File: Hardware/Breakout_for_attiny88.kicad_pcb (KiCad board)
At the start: 2 copper layers, 22.9 x 46.5 mm, 14 parts, among them J1 Conn_01x08, J2 Conn_01x08, J3 Conn_01x08, J4 AVR-ISP-6, J5 Conn_01x02, J6 Conn_01x02, SW1 SW, U1 ATT88

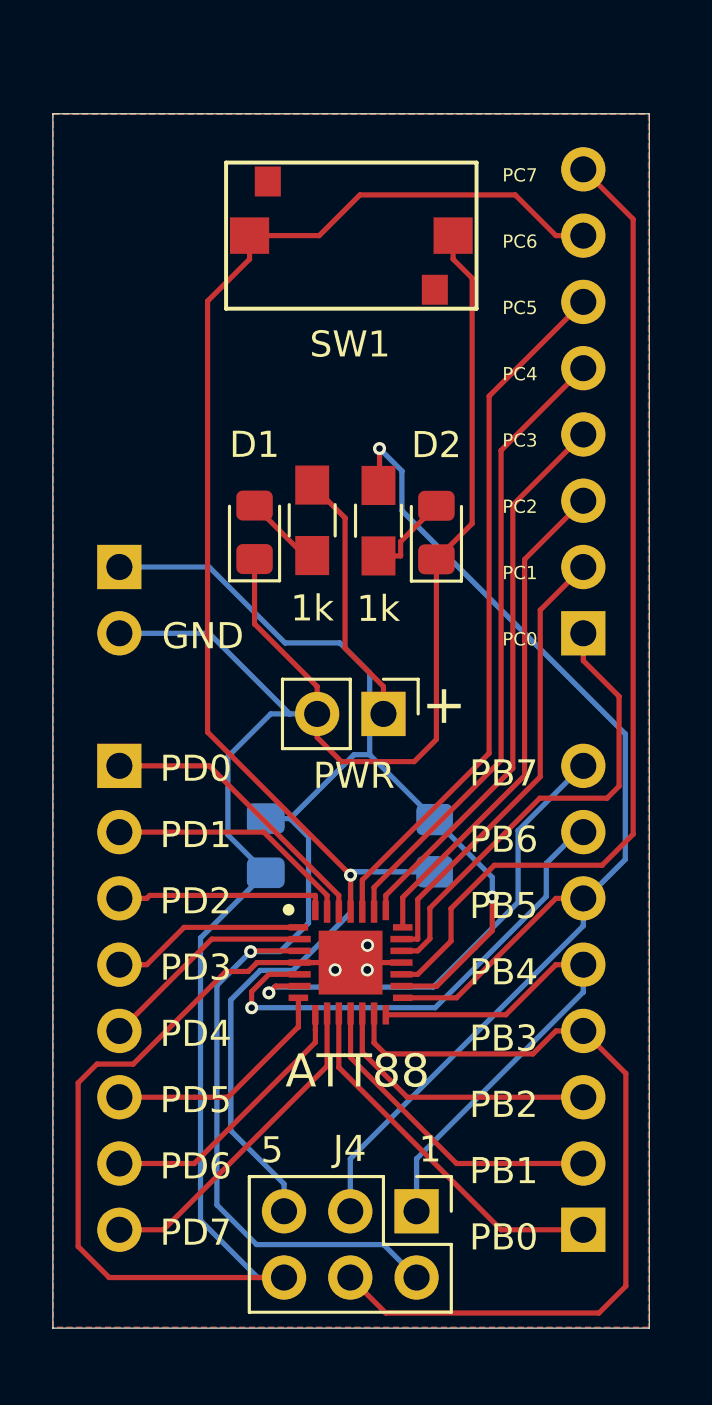
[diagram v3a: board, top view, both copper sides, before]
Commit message: pcb changed to add port pins on each header
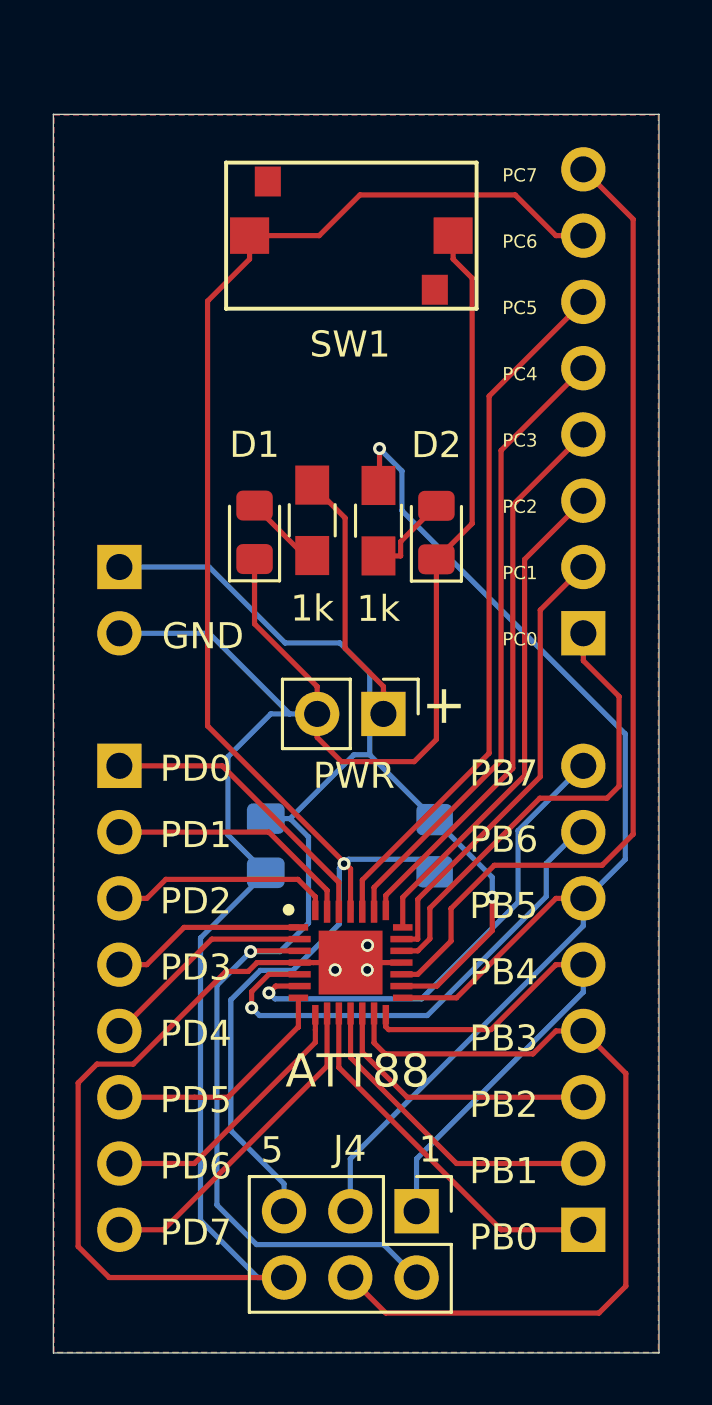
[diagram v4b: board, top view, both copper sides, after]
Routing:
- net PC6: track 62.6 -> 63.4 mm
- net MISO: track 20.5 -> 21.2 mm
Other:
- board size 22.9 x 46.5 mm -> 23.2 x 47.5 mm
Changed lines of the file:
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@@
     )
   )
-  (gr_line (start 137.06 126.55) (end 159.92 126.55) (layer "Edge.Cuts") (width 0.05))
-  (gr_line (start 159.92 80.01) (end 137.06 80.01) (layer "Edge.Cuts") (width 0.05))
-  (gr_line (start 137.06 80.01) (end 137.06 126.55) (layer "Edge.Cuts") (width 0.05))
-  (gr_line (start 159.92 80.01) (end 159.92 126.55) (layer "Edge.Cuts") (width 0.05))
+  (gr_rect (start 137.08 80.03) (end 160.29 127.5) (layer "Edge.Cuts") (width 0.0254) (fill none))
   (gr_text "PB4" (at 154.34 112.91) (layer "F.SilkS")
     (effects (font (size 1 1) (thickness 0.15)))
@@
   (segment (start 145.34 113.7) (end 145.6 113.44) (width 0.2) (layer "F.Cu") (net 9))
   (via (at 145.34 113.7) (size 0.5) (layers "F.Cu" "B.Cu") (net 9))
-  (segment (start 145.5622 113.4778) (end 145.34 113.7) (width 0.2) (layer "B.Cu") (net 9))
-  (segment (start 151.6422 113.4778) (end 145.5622 113.4778) (width 0.2) (layer "B.Cu") (net 9))
+  (segment (start 157.37 105) (end 154.89 107.48) (width 0.2) (layer "B.Cu") (net 9))
+  (segment (start 157.39 105) (end 157.37 105) (width 0.2) (layer "B.Cu") (net 9))
   (segment (start 154.89 107.48) (end 154.89 110.23) (width 0.2) (layer "B.Cu") (net 9))
-  (segment (start 157.39 105) (end 157.37 105) (width 0.2) (layer "B.Cu") (net 9))
-  (segment (start 157.37 105) (end 154.89 107.48) (width 0.2) (layer "B.Cu") (net 9))
-  (segment (start 154.89 110.23) (end 151.6422 113.4778) (width 0.2) (layer "B.Cu") (net 9))
+  (segment (start 145.57 113.93) (end 145.34 113.7) (width 0.2) (layer "B.Cu") (net 9))
+  (segment (start 151.19 113.93) (end 145.57 113.93) (width 0.2) (layer "B.Cu") (net 9))
+  (segment (start 154.89 110.23) (end 151.19 113.93) (width 0.2) (layer "B.Cu") (net 9))
   (segment (start 145.34 112.99) (end 144.68 113.65) (width 0.2) (layer "F.Cu") (net 10))
   (segment (start 144.68 113.65) (end 144.68 114.27) (width 0.2) (layer "F.Cu") (net 10))
   (segment (start 146.52 112.99) (end 145.34 112.99) (width 0.2) (layer "F.Cu") (net 10))
   (via (at 144.68 114.27) (size 0.5) (layers "F.Cu" "B.Cu") (net 10))
+  (segment (start 151.4103 114.57) (end 144.98 114.57) (width 0.2) (layer "B.Cu") (net 10))
+  (segment (start 155.97 108.74) (end 155.97 110.0103) (width 0.2) (layer "B.Cu") (net 10))
+  (segment (start 155.97 110.0103) (end 151.4103 114.57) (width 0.2) (layer "B.Cu") (net 10))
   (segment (start 157.39 107.54) (end 157.17 107.54) (width 0.2) (layer "B.Cu") (net 10))
+  (segment (start 144.98 114.57) (end 144.68 114.27) (width 0.2) (layer "B.Cu") (net 10))
   (segment (start 157.17 107.54) (end 155.97 108.74) (width 0.2) (layer "B.Cu") (net 10))
-  (segment (start 155.97 110.0103) (end 151.7103 114.27) (width 0.2) (layer "B.Cu") (net 10))
-  (segment (start 151.7103 114.27) (end 144.68 114.27) (width 0.2) (layer "B.Cu") (net 10))
-  (segment (start 155.97 108.74) (end 155.97 110.0103) (width 0.2) (layer "B.Cu") (net 10))
-  (segment (start 142.99 103.709) (end 142.99 87.1903) (width 0.2) (layer "F.Cu") (net 11))
+  (segment (start 148.47 108.95) (end 142.99 103.47) (width 0.2) (layer "F.Cu") (net 11))
+  (segment (start 144.6 85.5803) (end 144.6 84.68) (width 0.2) (layer "F.Cu") (net 11))
+  (segment (start 142.99 87.1903) (end 144.6 85.5803) (width 0.2) (layer "F.Cu") (net 11))
   (segment (start 157.39 84.68) (end 156.3397 84.68) (width 0.2) (layer "F.Cu") (net 11))
   (segment (start 156.3397 84.68) (end 154.7797 83.12) (width 0.2) (layer "F.Cu") (net 11))
-  (segment (start 144.6 85.5803) (end 144.6 84.68) (width 0.2) (layer "F.Cu") (net 11))
   (segment (start 147.27 84.68) (end 144.6 84.68) (width 0.2) (layer "F.Cu") (net 11))
-  (segment (start 148.47 110.59) (end 148.47 109.189) (width 0.2) (layer "F.Cu") (net 11))
   (segment (start 148.83 83.12) (end 147.27 84.68) (width 0.2) (layer "F.Cu") (net 11))
+  (segment (start 142.99 103.47) (end 142.99 87.1903) (width 0.2) (layer "F.Cu") (net 11))
+  (segment (start 148.47 110.59) (end 148.47 108.95) (width 0.2) (layer "F.Cu") (net 11))
   (segment (start 154.7797 83.12) (end 148.83 83.12) (width 0.2) (layer "F.Cu") (net 11))
-  (segment (start 142.99 87.1903) (end 144.6 85.5803) (width 0.2) (layer "F.Cu") (net 11))
-  (segment (start 148.47 109.189) (end 142.99 103.709) (width 0.2) (layer "F.Cu") (net 11))
-  (via (at 148.47 109.189) (size 0.5) (layers "F.Cu" "B.Cu") (net 11))
+  (via (at 148.22 108.75) (size 0.5) (layers "F.Cu" "B.Cu") (net 11))
   (segment (start 143.88 113.97) (end 143.88 118.9797) (width 0.2) (layer "B.Cu") (net 11))
   (segment (start 145.01 112.84) (end 143.88 113.97) (width 0.2) (layer "B.Cu") (net 11))
-  (segment (start 148.47 110.63) (end 146.26 112.84) (width 0.2) (layer "B.Cu") (net 11))
-  (segment (start 151.69 109.06) (end 148.599 109.06) (width 0.2) (layer "B.Cu") (net 11))
+  (segment (start 148.04 111.06) (end 146.26 112.84) (width 0.2) (layer "B.Cu") (net 11))
+  (segment (start 143.88 118.9797) (end 145.92 121.0197) (width 0.2) (layer "B.Cu") (net 11))
+  (segment (start 148.22 108.75) (end 148.04 108.93) (width 0.2) (layer "B.Cu") (net 11))
+  (segment (start 148.04 108.93) (end 148.04 111.06) (width 0.2) (layer "B.Cu") (net 11))
+  (segment (start 151.69 109.06) (end 151.21 108.58) (width 0.2) (layer "B.Cu") (net 11))
+  (segment (start 148.39 108.58) (end 148.22 108.75) (width 0.2) (layer "B.Cu") (net 11))
+  (segment (start 151.21 108.58) (end 148.39 108.58) (width 0.2) (layer "B.Cu") (net 11))
   (segment (start 145.92 121.0197) (end 145.92 122.07) (width 0.2) (layer "B.Cu") (net 11))
   (segment (start 146.26 112.84) (end 145.01 112.84) (width 0.2) (layer "B.Cu") (net 11))
-  (segment (start 148.599 109.06) (end 148.47 109.189) (width 0.2) (layer "B.Cu") (net 11))
-  (segment (start 148.47 109.189) (end 148.47 110.63) (width 0.2) (layer "B.Cu") (net 11))
-  (segment (start 143.88 118.9797) (end 145.92 121.0197) (width 0.2) (layer "B.Cu") (net 11))
-  (segment (start 149.82 114.54) (end 154.4197 114.54) (width 0.2) (layer "F.Cu") (net 12))
-  (segment (start 154.4197 114.54) (end 156.3397 112.62) (width 0.2) (layer "F.Cu") (net 12))
-  (segment (start 157.39 112.62) (end 156.3397 112.62) (width 0.2) (layer "F.Cu") (net 12))
+  (segment (start 149.82 115) (end 149.93 115.11) (width 0.2) (layer "F.Cu") (net 12))
+  (segment (start 153.8497 115.11) (end 156.3397 112.62) (width 0.2) (layer "F.Cu") (net 12))
+  (segment (start 156.3397 112.62) (end 157.39 112.62) (width 0.2) (layer "F.Cu") (net 12))
+  (segment (start 149.93 115.11) (end 153.8497 115.11) (width 0.2) (layer "F.Cu") (net 12))
+  (segment (start 149.82 114.54) (end 149.82 115) (width 0.2) (layer "F.Cu") (net 12))
   (segment (start 157.39 112.62) (end 157.39 113.6703) (width 0.2) (layer "B.Cu") (net 12))
   (segment (start 151 120.0603) (end 151 122.07) (width 0.2) (layer "B.Cu") (net 12))
@@
   (segment (start 139.61 112.62) (end 140.6603 112.62) (width 0.2) (layer "F.Cu") (net 22))
   (segment (start 142.0903 111.19) (end 146.47 111.19) (width 0.2) (layer "F.Cu") (net 22))
+  (segment (start 140.6603 110.08) (end 141.3903 109.35) (width 0.2) (layer "F.Cu") (net 23))
+  (segment (start 146.45 109.35) (end 147.12 110.02) (width 0.2) (layer "F.Cu") (net 23))
   (segment (start 139.61 110.08) (end 140.6603 110.08) (width 0.2) (layer "F.Cu") (net 23))
-  (segment (start 140.6603 110.08) (end 140.7756 109.9647) (width 0.2) (layer "F.Cu") (net 23))
-  (segment (start 140.7756 109.9647) (end 147.12 109.9647) (width 0.2) (layer "F.Cu") (net 23))
-  (segment (start 147.12 110.54) (end 147.12 109.9647) (width 0.2) (layer "F.Cu") (net 23))
-  (segment (start 145.1453 107.54) (end 147.57 109.9647) (width 0.2) (layer "F.Cu") (net 24))
-  (segment (start 147.57 110.59) (end 147.57 109.9647) (width 0.2) (layer "F.Cu") (net 24))
-  (segment (start 139.61 107.54) (end 145.1453 107.54) (width 0.2) (layer "F.Cu") (net 24))
-  (segment (start 139.61 105) (end 143.0553 105) (width 0.2) (layer "F.Cu") (net 25))
-  (segment (start 143.0553 105) (end 148.02 109.9647) (width 0.2) (layer "F.Cu") (net 25))
-  (segment (start 148.02 110.59) (end 148.02 109.9647) (width 0.2) (layer "F.Cu") (net 25))
+  (segment (start 141.3903 109.35) (end 146.45 109.35) (width 0.2) (layer "F.Cu") (net 23))
+  (segment (start 147.12 110.02) (end 147.12 110.54) (width 0.2) (layer "F.Cu") (net 23))
+  (segment (start 139.61 107.54) (end 145.34 107.54) (width 0.2) (layer "F.Cu") (net 24))
+  (segment (start 147.57 109.77) (end 147.57 110.59) (width 0.2) (layer "F.Cu") (net 24))
+  (segment (start 145.34 107.54) (end 147.57 109.77) (width 0.2) (layer "F.Cu") (net 24))
+  (segment (start 139.61 105) (end 143.55 105) (width 0.2) (layer "F.Cu") (net 25))
+  (segment (start 143.55 105) (end 148.02 109.47) (width 0.2) (layer "F.Cu") (net 25))
+  (segment (start 148.02 109.47) (end 148.02 110.59) (width 0.2) (layer "F.Cu") (net 25))
   (segment (start 152.32 111.7153) (end 151.0453 112.99) (width 0.2) (layer "F.Cu") (net 26))
   (segment (start 157.39 82.14) (end 159.3 84.05) (width 0.2) (layer "F.Cu") (net 26))
@@
     (polygon
       (pts
-        (xy 159.89 126.52)
-        (xy 137.08 126.52)
-        (xy 137.08 80.03)
-        (xy 159.89 80.03)
+        (xy 160.27 127.48)
+        (xy 137.1 127.48)
+        (xy 137.1 80.05)
+        (xy 160.27 80.05)
       )
     )
@@
     (polygon
       (pts
-        (xy 159.89 126.52)
-        (xy 137.08 126.52)
-        (xy 137.08 80.03)
-        (xy 159.89 80.03)
+        (xy 160.27 127.48)
+        (xy 137.1 127.48)
+        (xy 137.1 80.05)
+        (xy 160.27 80.05)
       )
     )
